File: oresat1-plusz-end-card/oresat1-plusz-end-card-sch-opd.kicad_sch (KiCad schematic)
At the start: 51 parts, among them Q1 DMP2240UDM, Q11 DMP2240UDM-7, Q2 PMV45EN, Q3 PMV45EN, Q4 PMV45EN, Q6 PMV45EN, Q9 DMP2240UDM-7, U11 MIC842LYC5, U12 MIC842LYC5, U2 MAX7310

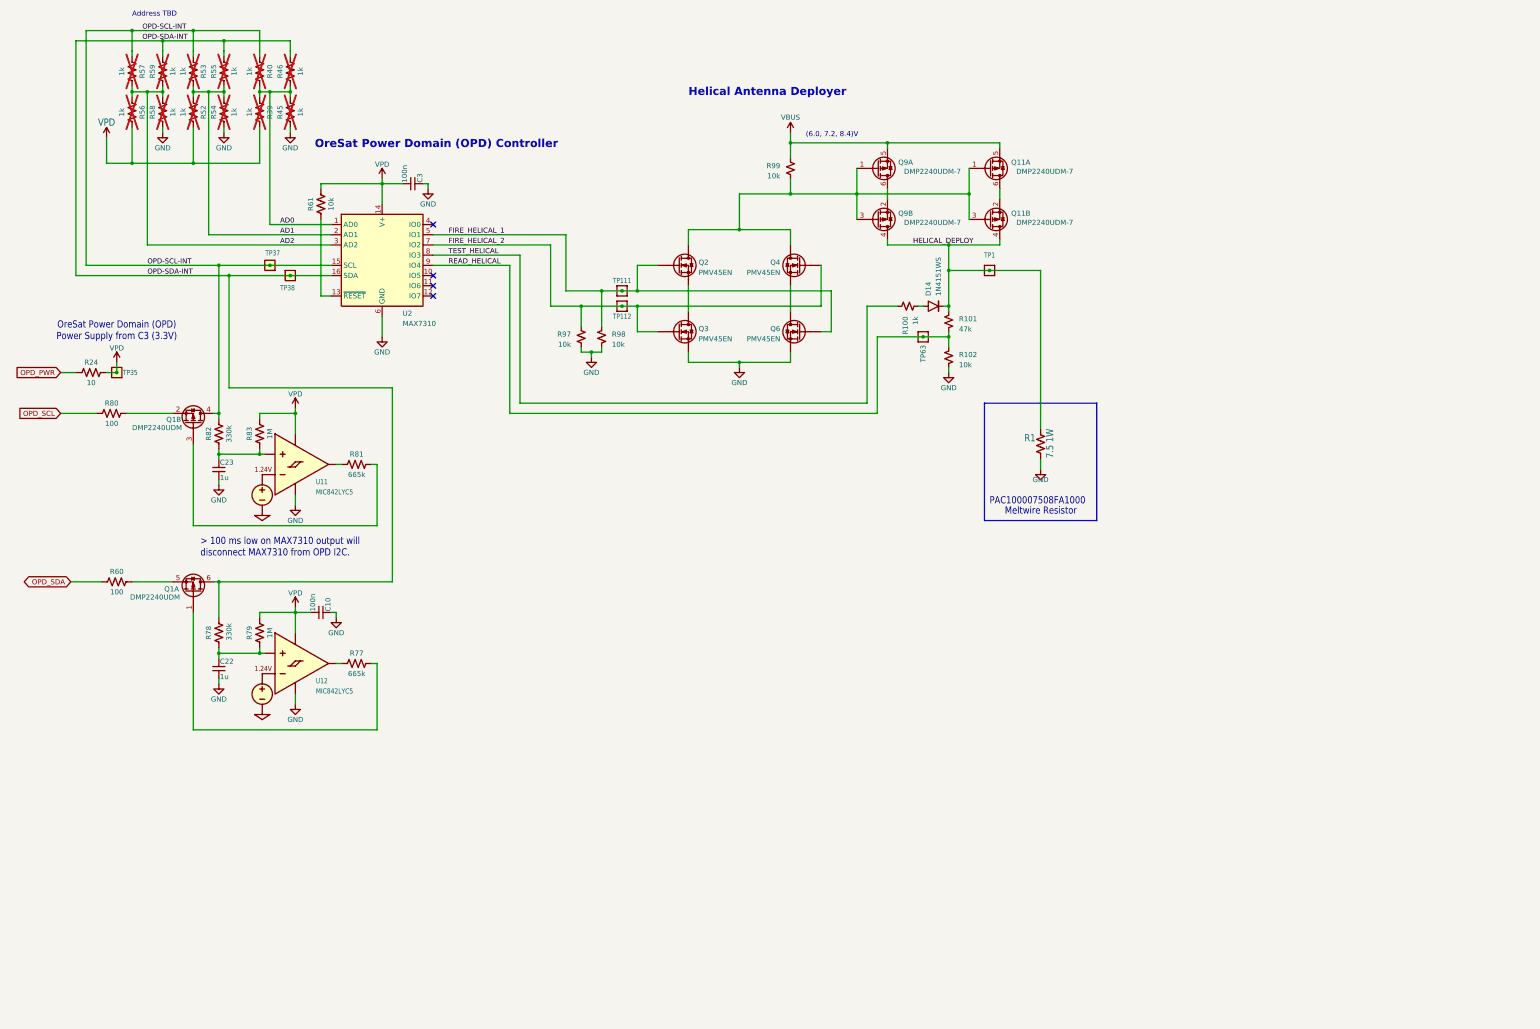
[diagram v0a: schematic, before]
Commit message: Changed symbols & fab layout
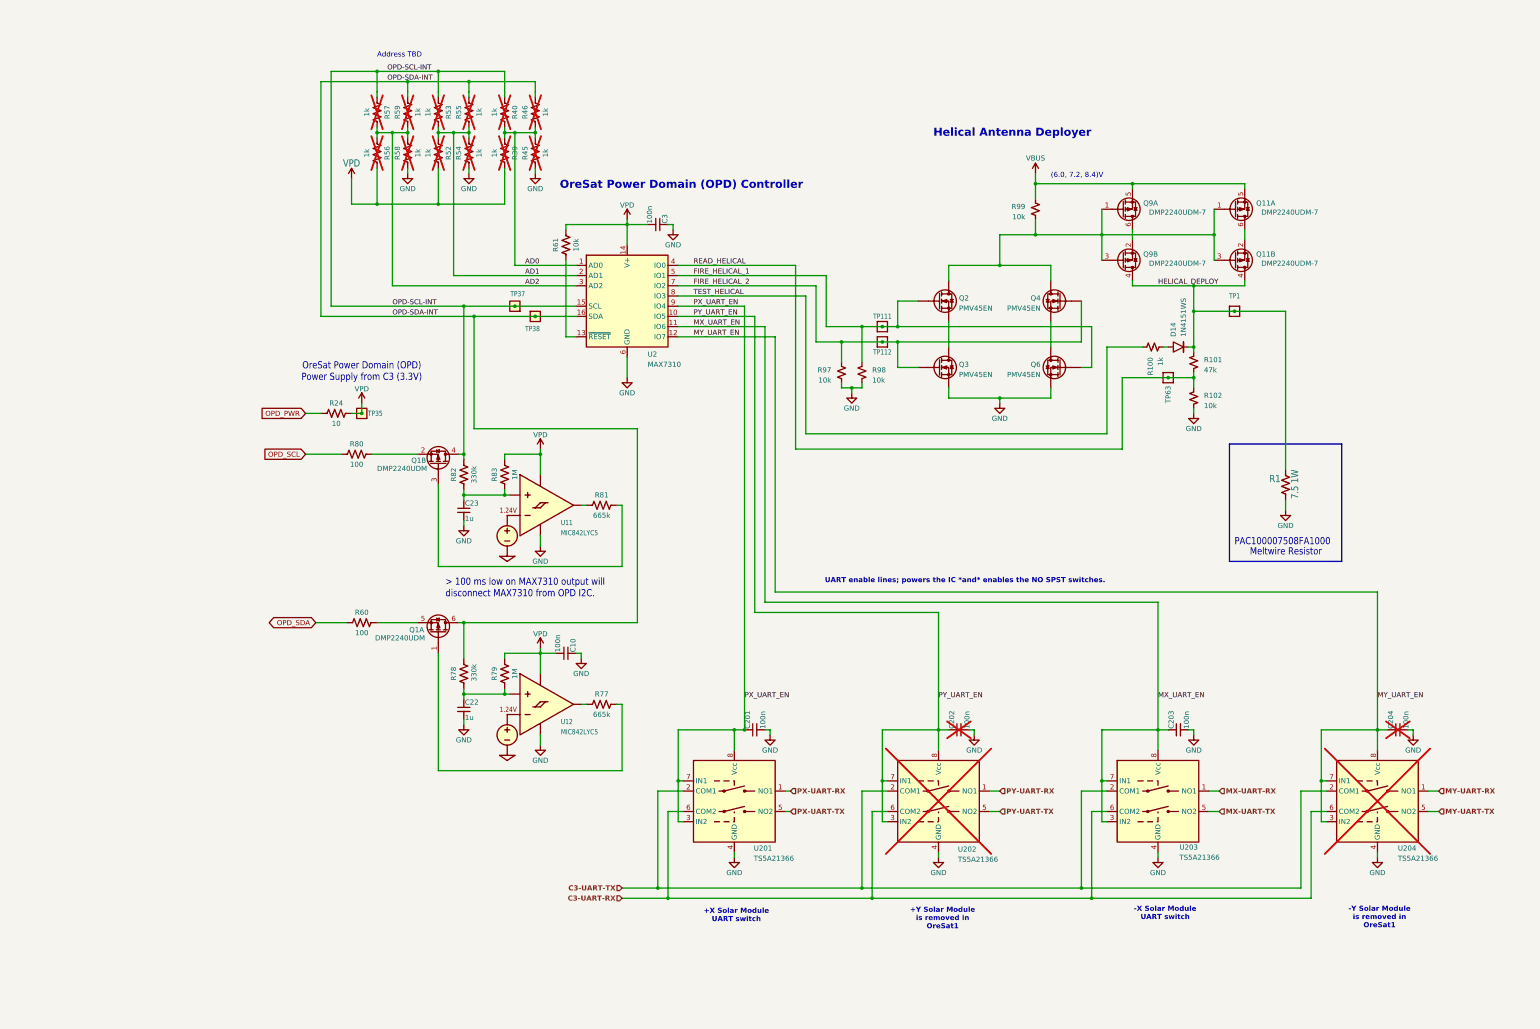
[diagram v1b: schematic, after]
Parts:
- added C201, C202, C203, C204: 100n, oresat-passives:0603-C-NOSILK, symbol Device:C_Small
- added U201, U202, U203, U204: TS5A21366, Package_SO:VSSOP-8_2.3x2mm_P0.5mm, symbol oresat-ics:TS5A21366
- D14: DST Digi-Key -> (none)
- R1: DIST DigiKey -> (none)
- R100, R101, R102, R97, R98, R99: DIS (none) -> DigiKey; DST Digi-Key -> (none)
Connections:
- net GND: now also C201.2, C202.2, C203.2, C204.2, U201.4 (GND), U202.4 (GND), U203.4 (GND), U204.4 (GND)
- net READ_HELICAL: now also U2.4 (IO0); no longer U2.9 (IO4)
- net PY_UART_EN: now reaches U2.10 (IO5)
- net PY_UART_EN: now also C202.1, U202.3 (IN2), U202.7 (IN1), U202.8 (Vcc)
- net MX_UART_EN: now reaches U2.11 (IO6)
- net MX_UART_EN: now also C203.1, U203.3 (IN2), U203.7 (IN1), U203.8 (Vcc)
- net MY_UART_EN: now reaches U2.12 (IO7)
- net MY_UART_EN: now also C204.1, U204.3 (IN2), U204.7 (IN1), U204.8 (Vcc)
- new net C3-UART-RX: U201.6 (COM2), U202.6 (COM2), U203.6 (COM2), U204.6 (COM2)
- new net C3-UART-TX: U201.2 (COM1), U202.2 (COM1), U203.2 (COM1), U204.2 (COM1)
- new net MX-UART-RX: U203.1 (NO1)
- new net MX-UART-TX: U203.5 (NO2)
- new net MY-UART-RX: U204.1 (NO1)
- new net MY-UART-TX: U204.5 (NO2)
- new net PX-UART-RX: U201.1 (NO1)
- new net PX-UART-TX: U201.5 (NO2)
- new net PX_UART_EN: C201.1, U2.9 (IO4), U201.3 (IN2), U201.7 (IN1), U201.8 (Vcc)
- new net PY-UART-RX: U202.1 (NO1)
- new net PY-UART-TX: U202.5 (NO2)
- no-connect marks 4 -> 0
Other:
- note added: "+X Solar Module UART switch"
- note added: "+Y Solar Module is removed in OreSat1"
- note added: "-X Solar Module UART switch"
- note added: "-Y Solar Module is removed in OreSat1"
- note added: "UART enable lines; powers the IC *and* enables the NO SPST switches."
- moved on the sheet: C10, C22, C23, C3, D14, Q11A, Q11B, Q1A, Q1B, Q2, Q3, Q4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

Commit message: bom finished
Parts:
- D14, R1: DIS (none) -> DigiKey

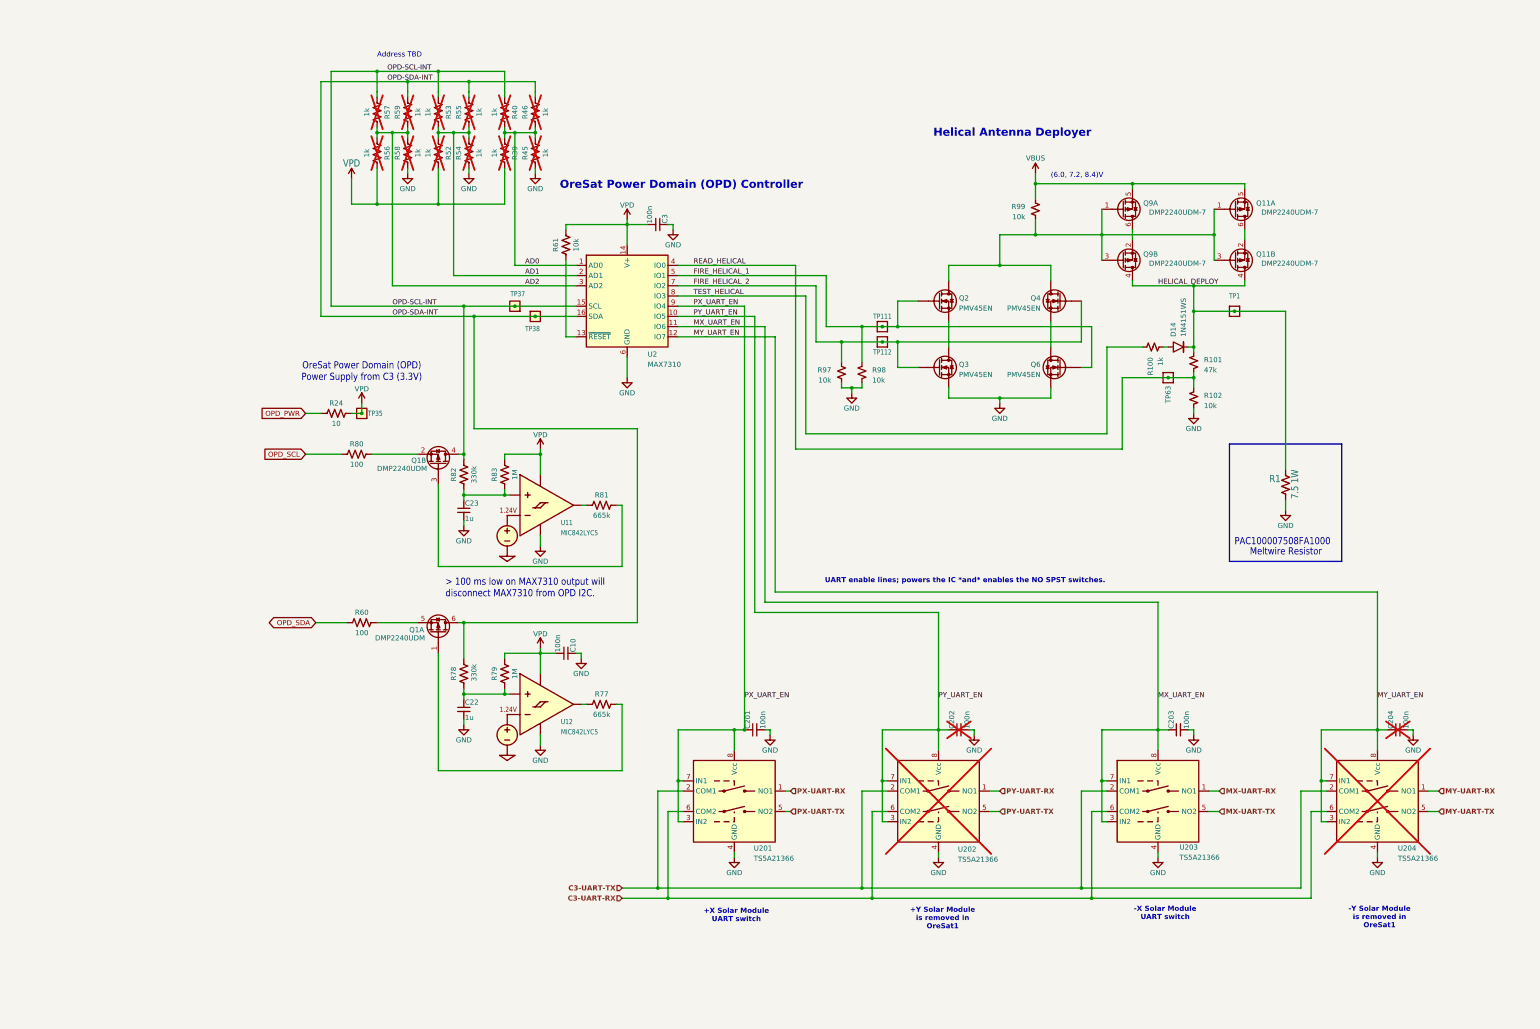
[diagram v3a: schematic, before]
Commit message: Fixed schematic label issues and routed solar uarts
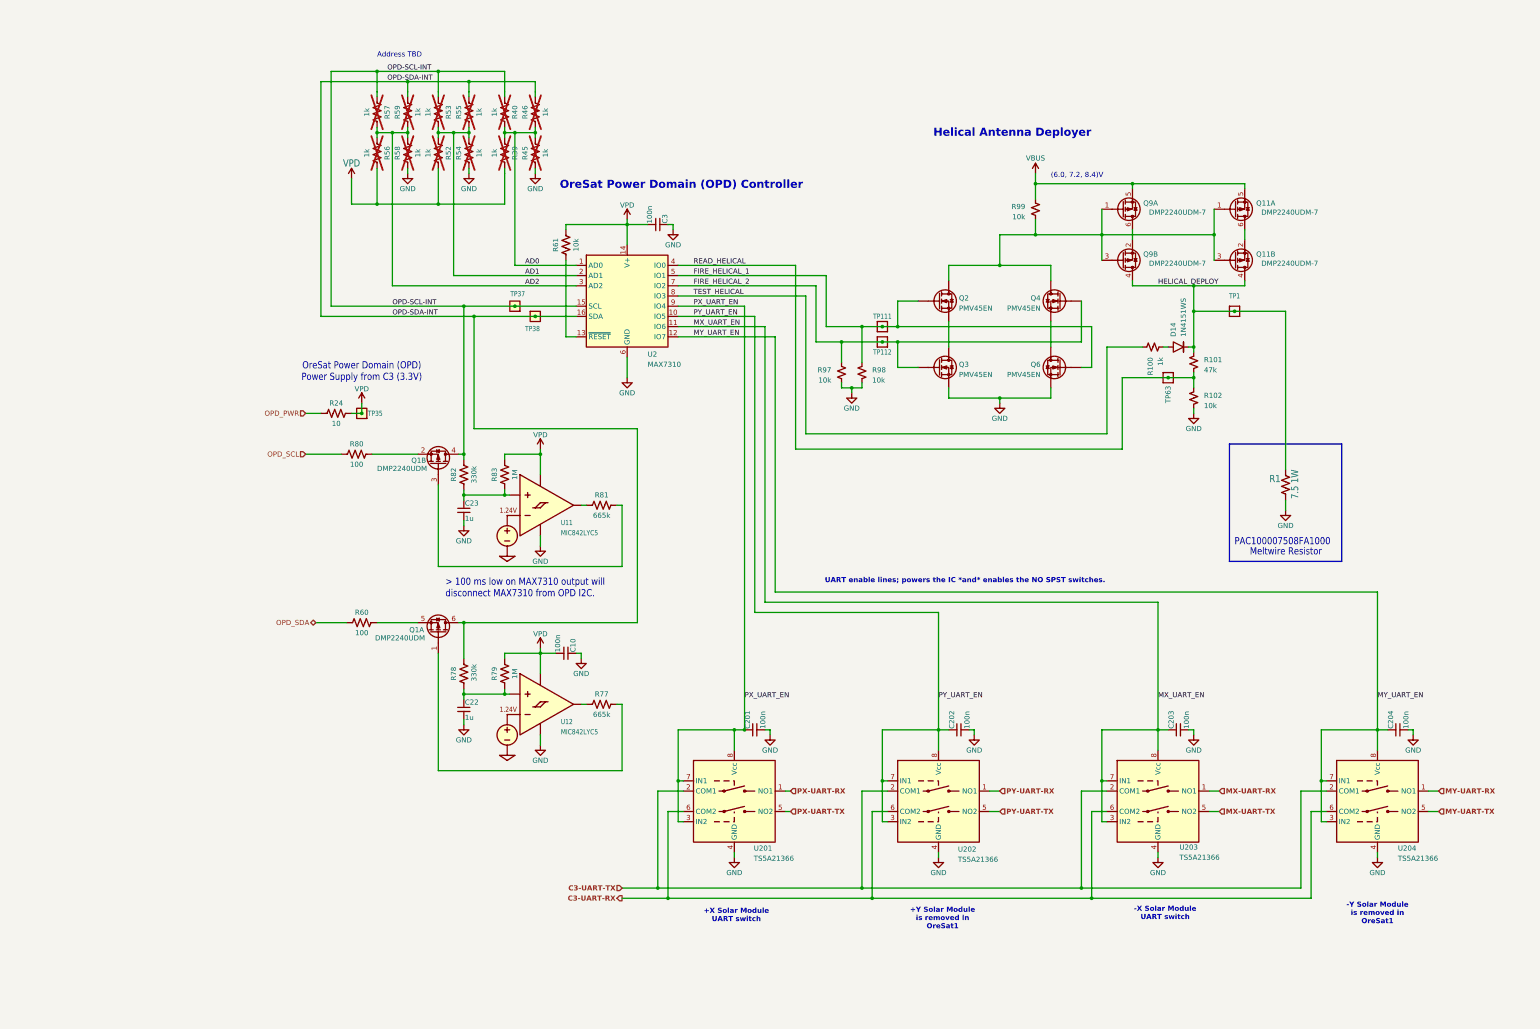
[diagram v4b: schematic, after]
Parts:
- C202, C204, U202, U204: now fitted
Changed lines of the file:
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@@
 	(text "-Y Solar Module \nis removed in \nOreSat1"
 		(exclude_from_sim no)
-		(at 353.568 239.776 0)
+		(at 353.06 238.76 0)
 		(effects
 			(font
@@
 		)
 	)
-	(global_label "OPD_SCL"
-		(shape input)
-		(at 86.36 124.46 180)
-		(fields_autoplaced yes)
-		(effects
-			(font
-				(size 1.27 1.27)
-			)
-			(justify right)
-		)
-		(property "Intersheetrefs" "${INTERSHEET_REFS}"
-			(at 75.0291 124.46 0)
-			(effects
-				(font
-					(size 1.27 1.27)
-				)
-				(justify right)
-				(hide yes)
-			)
-		)
-	)
-	(global_label "OPD_SDA"
-		(shape bidirectional)
-		(at 88.9 166.37 180)
-		(fields_autoplaced yes)
-		(effects
-			(font
-				(size 1.27 1.27)
-			)
-			(justify right)
-		)
-		(property "Intersheetrefs" "${INTERSHEET_REFS}"
-			(at 76.3973 166.37 0)
-			(effects
-				(font
-					(size 1.27 1.27)
-				)
-				(justify right)
-				(hide yes)
-			)
-		)
-	)
-	(global_label "OPD_PWR"
-		(shape input)
-		(at 86.36 114.3 180)
-		(fields_autoplaced yes)
-		(effects
-			(font
-				(size 1.27 1.27)
-			)
-			(justify right)
-		)
-		(property "Intersheetrefs" "${INTERSHEET_REFS}"
-			(at 74.5453 114.3 0)
-			(effects
-				(font
-					(size 1.27 1.27)
-				)
-				(justify right)
-				(hide yes)
-			)
-		)
-	)
 	(hierarchical_label "MX-UART-RX"
 		(shape input)
@@
 		)
 	)
+	(hierarchical_label "OPD_SDA"
+		(shape bidirectional)
+		(at 88.9 166.37 180)
+		(effects
+			(font
+				(size 1.27 1.27)
+			)
+			(justify right)
+		)
+	)
 	(hierarchical_label "MY-UART-TX"
 		(shape input)
@@
 		)
 	)
-	(hierarchical_label "C3-UART-RX"
+	(hierarchical_label "OPD_PWR"
 		(shape input)
+		(at 86.36 114.3 180)
+		(effects
+			(font
+				(size 1.27 1.27)
+			)
+			(justify right)
+		)
+	)
+	(hierarchical_label "OPD_SCL"
+		(shape input)
+		(at 86.36 124.46 180)
+		(effects
+			(font
+				(size 1.27 1.27)
+			)
+			(justify right)
+		)
+	)
+	(hierarchical_label "C3-UART-RX"
+		(shape output)
 		(at 165.1 234.95 180)
 		(effects
@@
 	)
 	(symbol
-		(lib_name "TS5A21366_1")
 		(lib_id "oresat-ics:TS5A21366")
 		(at 243.84 210.82 0)
@@
 		(in_bom yes)
 		(on_board yes)
-		(dnp yes)
+		(dnp no)
 		(property "Reference" "U202"
 			(at 248.666 222.758 0)
@@
 	)
 	(symbol
-		(lib_name "TS5A21366_1")
 		(lib_id "oresat-ics:TS5A21366")
 		(at 353.06 210.82 0)
@@
 		(in_bom yes)
 		(on_board yes)
-		(dnp yes)
+		(dnp no)
 		(property "Reference" "U204"
 			(at 358.14 222.504 0)
@@
 		(in_bom yes)
 		(on_board yes)
-		(dnp yes)
+		(dnp no)
 		(property "Reference" "C204"
 			(at 356.362 192.786 0)
@@
 		(in_bom yes)
 		(on_board yes)
-		(dnp yes)
+		(dnp no)
 		(property "Reference" "C202"
 			(at 247.142 192.786 0)
@@
 	)
 	(symbol
-		(lib_name "TS5A21366_1")
 		(lib_id "oresat-ics:TS5A21366")
 		(at 298.45 210.82 0)
@@
 	)
 	(symbol
-		(lib_name "TS5A21366_1")
 		(lib_id "oresat-ics:TS5A21366")
 		(at 193.04 210.82 0)

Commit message: Another round on the +Z End Card; ready for fab.
Brushed up RF paths and solder mask, cleaned up UART switches with closer bypass caps, cleaned up a lot of the zones, and lots of little polishing.
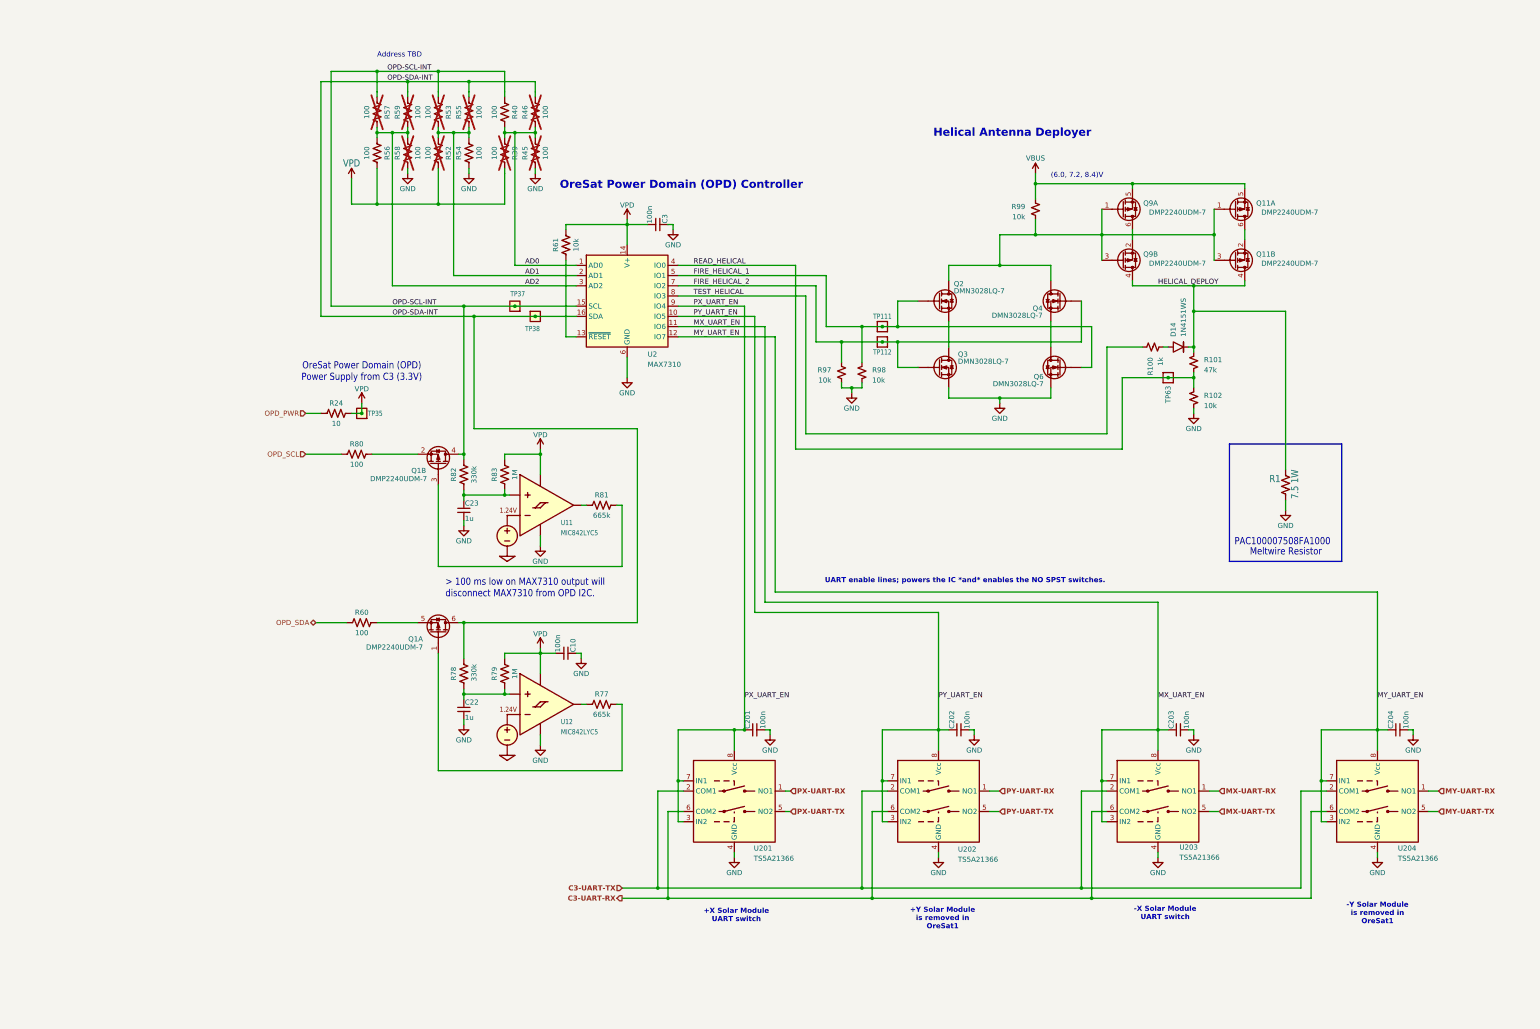
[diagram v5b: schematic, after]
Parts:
- removed TP1: Test-Point, oresat-misc:TestPoint_Pad_D1.0mm, symbol oresat-misc:Test-Point-1mm-round
- Q1: value DMP2240UDM -> DMP2240UDM-7; MPN DMP2240UDM -> DMP2240UDM-7
- Q11, Q9: MPN DMP2240UDM -> DMP2240UDM-7
- Q2, Q3, Q4, Q6: value PMV45EN -> DMN3028LQ-7; DIS Digi-Key -> DigiKey; DPN 1727-2307-1-ND -> 31-DMN3028LQ-7CT-ND; MFR Nexperia -> Diodes Incorporated; MPN PMV45EN2R -> DMN3028LQ-7
- R1: DPN 749-PAC100007508FA1000TB-ND -> 749-PAC100007508FA1000CT-ND; MFR Vishay Beyschlag/Draloric/BC Components -> Vishay
- R39, R45, R46, R52, R53, R55, R57, R59: value 1k -> 100; DIS Digi-Key -> DigiKey; DPN 1276-4275-1-ND -> RMCF0603FT100RCT-ND; MFR Samsung -> Stackpole Electronics Inc; MPN RC1005F6653CS -> RMCF0603FT100R
- R40, R54: value 1k -> 100; DPN RMCF0603FT1K00CT-ND -> RMCF0603FT100RCT-ND; MPN RMCF0603FT1K00 -> RMCF0603FT100R; now fitted
- R56: value 1k -> 100; DIS Digi-Key -> DigiKey; DPN 1276-4275-1-ND -> RMCF0603FT100RCT-ND; MFR Samsung -> Stackpole Electronics Inc; MPN RC1005F6653CS -> RMCF0603FT100R; now fitted
- R58: value 1k -> 100; DPN RMCF0603FT1K00CT-ND -> RMCF0603FT100RCT-ND; MPN RMCF0603FT1K00 -> RMCF0603FT100R
- U2: MFR Maxim -> Analog Devices; MPN MAX7310ATE -> MAX7310ATE+
